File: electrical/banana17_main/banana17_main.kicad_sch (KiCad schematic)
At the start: 26 parts, among them J1 78171-0004, U1 RP2040, U2 NCP1117-3.3_SOT223, U3 ssd1306_128x32, U4 W25Q128JVS, Y1 ABMB-272-T3

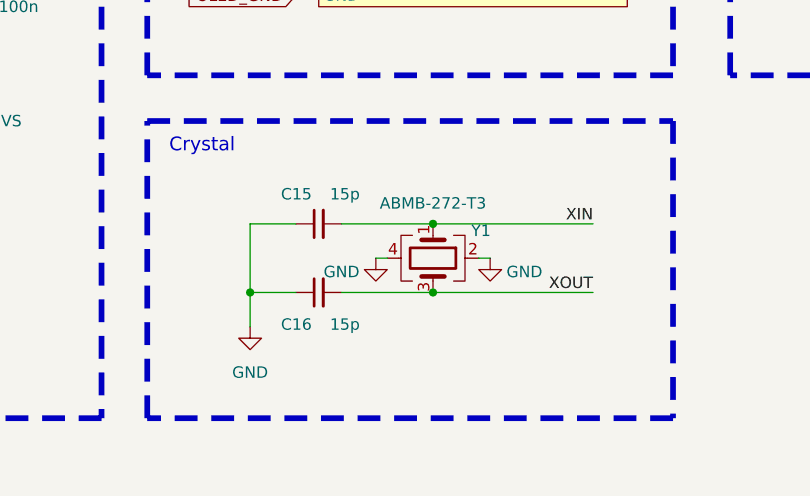
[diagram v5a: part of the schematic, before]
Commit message: MX footprint updated with hotswappable socket.
MX footprint updated with hotswappable socket. Some issues with KiCAD plugin for keyboard layout editor, switches not aligning.
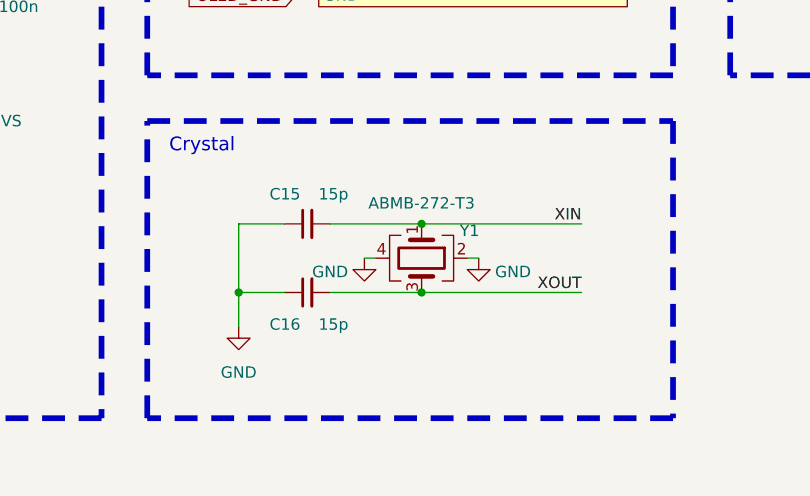
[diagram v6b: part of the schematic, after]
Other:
- moved on the sheet: C15, C16, Y1
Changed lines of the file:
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@@
 	)
 	(junction
-		(at 132.08 166.37)
+		(at 130.81 166.37)
 		(diameter 0)
 		(color 0 0 0 0)
@@
 	)
 	(junction
-		(at 132.08 173.99)
+		(at 130.81 173.99)
 		(diameter 0)
 		(color 0 0 0 0)
@@
 	)
 	(junction
-		(at 111.76 173.99)
+		(at 110.49 173.99)
 		(diameter 0)
 		(color 0 0 0 0)
@@
 	(wire
 		(pts
-			(xy 132.08 173.99) (xy 149.86 173.99)
+			(xy 130.81 173.99) (xy 148.59 173.99)
 		)
 		(stroke
@@
 	(wire
 		(pts
-			(xy 111.76 173.99) (xy 111.76 166.37)
+			(xy 110.49 173.99) (xy 110.49 166.37)
 		)
 		(stroke
@@
 	(wire
 		(pts
-			(xy 132.08 166.37) (xy 149.86 166.37)
+			(xy 130.81 166.37) (xy 148.59 166.37)
 		)
 		(stroke
@@
 	(wire
 		(pts
-			(xy 111.76 173.99) (xy 111.76 177.8)
+			(xy 110.49 173.99) (xy 110.49 177.8)
 		)
 		(stroke
@@
 	(wire
 		(pts
-			(xy 121.92 173.99) (xy 132.08 173.99)
+			(xy 120.65 173.99) (xy 130.81 173.99)
 		)
 		(stroke
@@
 	(wire
 		(pts
-			(xy 137.16 170.18) (xy 138.43 170.18)
+			(xy 135.89 170.18) (xy 137.16 170.18)
 		)
 		(stroke
@@
 	(wire
 		(pts
-			(xy 111.76 166.37) (xy 116.84 166.37)
+			(xy 110.49 166.37) (xy 115.57 166.37)
 		)
 		(stroke
@@
 	(wire
 		(pts
-			(xy 116.84 173.99) (xy 111.76 173.99)
+			(xy 115.57 173.99) (xy 110.49 173.99)
 		)
 		(stroke
@@
 	(wire
 		(pts
-			(xy 127 170.18) (xy 125.73 170.18)
+			(xy 125.73 170.18) (xy 124.46 170.18)
 		)
 		(stroke
@@
 	(wire
 		(pts
-			(xy 121.92 166.37) (xy 132.08 166.37)
+			(xy 120.65 166.37) (xy 130.81 166.37)
 		)
 		(stroke
@@
 	)
 	(label "XOUT"
-		(at 149.86 173.99 180)
+		(at 148.59 173.99 180)
 		(fields_autoplaced yes)
 		(effects
@@
 	)
 	(label "XIN"
-		(at 149.86 166.37 180)
+		(at 148.59 166.37 180)
 		(fields_autoplaced yes)
 		(effects
@@
 	(symbol
 		(lib_id "Device:Crystal_GND24")
-		(at 132.08 170.18 270)
+		(at 130.81 170.18 270)
 		(unit 1)
 		(exclude_from_sim no)
@@
 		(dnp no)
 		(property "Reference" "Y1"
-			(at 137.414 167.132 90)
+			(at 136.144 167.132 90)
 			(effects
 				(font
@@
 		)
 		(property "Value" "ABMB-272-T3"
-			(at 132.08 164.084 90)
+			(at 130.81 164.084 90)
 			(effects
 				(font
@@
 		)
 		(property "Footprint" "Crystal:Crystal_SMD_Abracon_ABM8G-4Pin_3.2x2.5mm"
-			(at 132.08 170.18 0)
+			(at 130.81 170.18 0)
 			(effects
 				(font
@@
 		)
 		(property "Datasheet" "~"
-			(at 132.08 170.18 0)
+			(at 130.81 170.18 0)
 			(effects
 				(font
@@
 		)
 		(property "Description" "Four pin crystal, GND on pins 2 and 4"
-			(at 132.08 170.18 0)
+			(at 130.81 170.18 0)
 			(effects
 				(font
@@
 	(symbol
 		(lib_id "power:GND")
-		(at 111.76 177.8 0)
+		(at 110.49 177.8 0)
 		(unit 1)
 		(exclude_from_sim no)
@@
 		(dnp no)
 		(property "Reference" "#PWR021"
-			(at 111.76 184.15 0)
+			(at 110.49 184.15 0)
 			(effects
 				(font
@@
 		)
 		(property "Value" "GND"
-			(at 111.76 182.88 0)
+			(at 110.49 182.88 0)
 			(effects
 				(font
@@
 		)
 		(property "Footprint" ""
-			(at 111.76 177.8 0)
+			(at 110.49 177.8 0)
 			(effects
 				(font
@@
 		)
 		(property "Datasheet" ""
-			(at 111.76 177.8 0)
+			(at 110.49 177.8 0)
 			(effects
 				(font
@@
 		)
 		(property "Description" "Power symbol creates a global label with name \"GND\" , ground"
-			(at 111.76 177.8 0)
+			(at 110.49 177.8 0)
 			(effects
 				(font
@@
 	(symbol
 		(lib_id "power:GND")
-		(at 138.43 170.18 0)
+		(at 137.16 170.18 0)
 		(unit 1)
 		(exclude_from_sim no)
@@
 		(dnp no)
 		(property "Reference" "#PWR018"
-			(at 138.43 176.53 0)
+			(at 137.16 176.53 0)
 			(effects
 				(font
@@
 		)
 		(property "Value" "GND"
-			(at 142.24 171.704 0)
+			(at 140.97 171.704 0)
 			(effects
 				(font
@@
 		)
 		(property "Footprint" ""
-			(at 138.43 170.18 0)
+			(at 137.16 170.18 0)
 			(effects
 				(font
@@
 		)
 		(property "Datasheet" ""
-			(at 138.43 170.18 0)
+			(at 137.16 170.18 0)
 			(effects
 				(font
@@
 		)
 		(property "Description" "Power symbol creates a global label with name \"GND\" , ground"
-			(at 138.43 170.18 0)
+			(at 137.16 170.18 0)
 			(effects
 				(font
@@
 	(symbol
 		(lib_id "power:GND")
-		(at 125.73 170.18 0)
+		(at 124.46 170.18 0)
 		(mirror y)
 		(unit 1)
@@
 		(dnp no)
 		(property "Reference" "#PWR017"
-			(at 125.73 176.53 0)
+			(at 124.46 176.53 0)
 			(effects
 				(font
@@
 		)
 		(property "Value" "GND"
-			(at 121.92 171.704 0)
+			(at 120.65 171.704 0)
 			(effects
 				(font
@@
 		)
 		(property "Footprint" ""
-			(at 125.73 170.18 0)
+			(at 124.46 170.18 0)
 			(effects
 				(font
@@
 		)
 		(property "Datasheet" ""
-			(at 125.73 170.18 0)
+			(at 124.46 170.18 0)
 			(effects
 				(font
@@
 		)
 		(property "Description" "Power symbol creates a global label with name \"GND\" , ground"
-			(at 125.73 170.18 0)
+			(at 124.46 170.18 0)
 			(effects
 				(font
@@
 	(symbol
 		(lib_id "Device:C_Small")
-		(at 119.38 166.37 90)
+		(at 118.11 166.37 90)
 		(unit 1)
 		(exclude_from_sim no)
@@
 		(dnp no)
 		(property "Reference" "C15"
-			(at 118.618 163.068 90)
+			(at 117.348 163.068 90)
 			(effects
 				(font
@@
 		)
 		(property "Value" "15p"
-			(at 123.952 163.068 90)
+			(at 122.682 163.068 90)
 			(effects
 				(font
@@
 		)
 		(property "Footprint" "Capacitor_SMD:C_0805_2012Metric_Pad1.18x1.45mm_HandSolder"
-			(at 119.38 166.37 0)
+			(at 118.11 166.37 0)
 			(effects
 				(font
@@
 		)
 		(property "Datasheet" "~"
-			(at 119.38 166.37 0)
+			(at 118.11 166.37 0)
 			(effects
 				(font
@@
 		)
 		(property "Description" "Unpolarized capacitor, small symbol"
-			(at 119.38 166.37 0)
+			(at 118.11 166.37 0)
 			(effects
 				(font
@@
 	(symbol
 		(lib_id "Device:C_Small")
-		(at 119.38 173.99 90)
+		(at 118.11 173.99 90)
 		(unit 1)
 		(exclude_from_sim no)
@@
 		(dnp no)
 		(property "Reference" "C16"
-			(at 118.618 177.546 90)
+			(at 117.348 177.546 90)
 			(effects
 				(font
@@
 		)
 		(property "Value" "15p"
-			(at 123.952 177.546 90)
+			(at 122.682 177.546 90)
 			(effects
 				(font
@@
 		)
 		(property "Footprint" "Capacitor_SMD:C_0805_2012Metric_Pad1.18x1.45mm_HandSolder"
-			(at 119.38 173.99 0)
+			(at 118.11 173.99 0)
 			(effects
 				(font
@@
 		)
 		(property "Datasheet" "~"
-			(at 119.38 173.99 0)
+			(at 118.11 173.99 0)
 			(effects
 				(font
@@
 		)
 		(property "Description" "Unpolarized capacitor, small symbol"
-			(at 119.38 173.99 0)
+			(at 118.11 173.99 0)
 			(effects
 				(font

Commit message: Switches positioned in matrix. Working on positioning the RP2040.
Switches positioned in matrix. Working on positioning the RP2040.
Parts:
- C1, C10, C11, C2, C3, C4, C5, C6, C7, C8, C9: footprint Capacitor_SMD:C_0805_2012Metric_Pad1.18x1.45mm_HandSolder -> Capacitor_SMD:C_0402_1005Metric_Pad0.74x0.62mm_HandSolder
- R1, R2: footprint Resistor_SMD:R_0805_2012Metric_Pad1.20x1.40mm_HandSolder -> Resistor_SMD:R_0402_1005Metric_Pad0.72x0.64mm_HandSolder
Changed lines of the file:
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@@
 	)
 	(junction
-		(at 135.89 46.99)
-		(diameter 0)
-		(color 0 0 0 0)
-	)
-	(junction
 		(at 105.41 39.37)
 		(diameter 0)
@@
 	)
 	(junction
-		(at 135.89 39.37)
+		(at 135.89 46.99)
 		(diameter 0)
 		(color 0 0 0 0)
@@
 		(color 0 0 0 0)
 	)
+	(junction
+		(at 135.89 39.37)
+		(diameter 0)
+		(color 0 0 0 0)
+	)
 	(wire
 		(pts
@@
 	(wire
 		(pts
+			(xy 135.89 46.99) (xy 146.05 46.99)
+		)
+		(stroke
+			(width 0)
+			(type default)
+		)
+	)
+	(wire
+		(pts
 			(xy 130.81 173.99) (xy 148.59 173.99)
 		)
@@
 	(wire
 		(pts
-			(xy 146.05 40.64) (xy 146.05 39.37)
-		)
-		(stroke
-			(width 0)
-			(type default)
-		)
-	)
-	(wire
-		(pts
 			(xy 248.92 60.96) (xy 265.43 60.96)
 		)
@@
 	(wire
 		(pts
-			(xy 146.05 39.37) (xy 135.89 39.37)
-		)
-		(stroke
-			(width 0)
-			(type default)
-		)
-	)
-	(wire
-		(pts
 			(xy 55.88 39.37) (xy 55.88 40.64)
 		)
@@
 	(wire
 		(pts
+			(xy 135.89 39.37) (xy 146.05 39.37)
+		)
+		(stroke
+			(width 0)
+			(type default)
+		)
+	)
+	(wire
+		(pts
 			(xy 45.72 39.37) (xy 45.72 40.64)
 		)
@@
 	(wire
 		(pts
+			(xy 146.05 39.37) (xy 146.05 40.64)
+		)
+		(stroke
+			(width 0)
+			(type default)
+		)
+	)
+	(wire
+		(pts
 			(xy 81.28 135.89) (xy 66.04 135.89)
 		)
@@
 	(wire
 		(pts
+			(xy 146.05 45.72) (xy 146.05 46.99)
+		)
+		(stroke
+			(width 0)
+			(type default)
+		)
+	)
+	(wire
+		(pts
 			(xy 110.49 36.83) (xy 110.49 39.37)
 		)
@@
 	(wire
 		(pts
-			(xy 135.89 46.99) (xy 146.05 46.99)
-		)
-		(stroke
-			(width 0)
-			(type default)
-		)
-	)
-	(wire
-		(pts
 			(xy 76.2 39.37) (xy 76.2 40.64)
 		)
@@
 	(wire
 		(pts
-			(xy 146.05 46.99) (xy 146.05 45.72)
-		)
-		(stroke
-			(width 0)
-			(type default)
-		)
-	)
-	(wire
-		(pts
 			(xy 248.92 121.92) (xy 265.43 121.92)
 		)
@@
 			)
 		)
-		(property "Footprint" "Capacitor_SMD:C_0805_2012Metric_Pad1.18x1.45mm_HandSolder"
+		(property "Footprint" "Capacitor_SMD:C_0402_1005Metric_Pad0.74x0.62mm_HandSolder"
 			(at 96.52 43.18 0)
 			(effects
@@
 			)
 		)
-		(property "Footprint" "Capacitor_SMD:C_0805_2012Metric_Pad1.18x1.45mm_HandSolder"
+		(property "Footprint" "Capacitor_SMD:C_0402_1005Metric_Pad0.74x0.62mm_HandSolder"
 			(at 105.41 43.18 0)
 			(effects
@@
 			)
 		)
-		(property "Footprint" "Capacitor_SMD:C_0805_2012Metric_Pad1.18x1.45mm_HandSolder"
+		(property "Footprint" "Capacitor_SMD:C_0402_1005Metric_Pad0.74x0.62mm_HandSolder"
 			(at 55.88 43.18 0)
 			(effects
@@
 			)
 		)
-		(property "Footprint" "Capacitor_SMD:C_0805_2012Metric_Pad1.18x1.45mm_HandSolder"
+		(property "Footprint" "Capacitor_SMD:C_0402_1005Metric_Pad0.74x0.62mm_HandSolder"
 			(at 115.57 43.18 0)
 			(effects
@@
 			)
 		)
-		(property "Footprint" "Resistor_SMD:R_0805_2012Metric_Pad1.20x1.40mm_HandSolder"
+		(property "Footprint" "Resistor_SMD:R_0402_1005Metric_Pad0.72x0.64mm_HandSolder"
 			(at 186.69 55.88 0)
 			(effects
@@
 			)
 		)
-		(property "Footprint" "Resistor_SMD:R_0805_2012Metric_Pad1.20x1.40mm_HandSolder"
+		(property "Footprint" "Resistor_SMD:R_0402_1005Metric_Pad0.72x0.64mm_HandSolder"
 			(at 186.69 58.42 0)
 			(effects
@@
 	)
 	(symbol
+		(lib_id "Device:C_Small")
+		(at 146.05 43.18 0)
+		(unit 1)
+		(exclude_from_sim no)
+		(in_bom yes)
+		(on_board yes)
+		(dnp no)
+		(property "Reference" "C11"
+			(at 148.59 41.9162 0)
+			(effects
+				(font
+					(size 1.27 1.27)
+				)
+				(justify left)
+			)
+		)
+		(property "Value" "100n"
+			(at 148.59 44.45 0)
+			(effects
+				(font
+					(size 1.27 1.27)
+				)
+				(justify left)
+			)
+		)
+		(property "Footprint" "Capacitor_SMD:C_0402_1005Metric_Pad0.74x0.62mm_HandSolder"
+			(at 146.05 43.18 0)
+			(effects
+				(font
+					(size 1.27 1.27)
+				)
+				(hide yes)
+			)
+		)
+		(property "Datasheet" "~"
+			(at 146.05 43.18 0)
+			(effects
+				(font
+					(size 1.27 1.27)
+				)
+				(hide yes)
+			)
+		)
+		(property "Description" "Unpolarized capacitor, small symbol"
+			(at 146.05 43.18 0)
+			(effects
+				(font
+					(size 1.27 1.27)
+				)
+				(hide yes)
+			)
+		)
+		(pin "1"
+		)
+		(pin "2"
+		)
+		(instances
+			(project "banana17_main"
+				(path "/fd2b462c-d7c2-4bbf-9a41-8b3fef737a65"
+					(reference "C11")
+					(unit 1)
+				)
+			)
+		)
+	)
+	(symbol
 		(lib_id "power:VBUS")
 		(at 139.7 87.63 0)
@@
 			)
 		)
-		(property "Footprint" "Capacitor_SMD:C_0805_2012Metric_Pad1.18x1.45mm_HandSolder"
+		(property "Footprint" "Capacitor_SMD:C_0402_1005Metric_Pad0.74x0.62mm_HandSolder"
 			(at 35.56 43.18 0)
 			(effects
@@
 			)
 		)
-		(property "Footprint" "Capacitor_SMD:C_0805_2012Metric_Pad1.18x1.45mm_HandSolder"
+		(property "Footprint" "Capacitor_SMD:C_0402_1005Metric_Pad0.74x0.62mm_HandSolder"
 			(at 86.36 43.18 0)
 			(effects
@@
 	)
 	(symbol
-		(lib_id "Device:C_Small")
-		(at 146.05 43.18 0)
-		(unit 1)
-		(exclude_from_sim no)
-		(in_bom yes)
-		(on_board yes)
-		(dnp no)
-		(property "Reference" "C11"
-			(at 148.59 41.9162 0)
-			(effects
-				(font
-					(size 1.27 1.27)
-				)
-				(justify left)
-			)
-		)
-		(property "Value" "100n"
-			(at 148.59 44.45 0)
-			(effects
-				(font
-					(size 1.27 1.27)
-				)
-				(justify left)
-			)
-		)
-		(property "Footprint" "Capacitor_SMD:C_0805_2012Metric_Pad1.18x1.45mm_HandSolder"
-			(at 146.05 43.18 0)
-			(effects
-				(font
-					(size 1.27 1.27)
-				)
-				(hide yes)
-			)
-		)
-		(property "Datasheet" "~"
-			(at 146.05 43.18 0)
-			(effects
-				(font
-					(size 1.27 1.27)
-				)
-				(hide yes)
-			)
-		)
-		(property "Description" "Unpolarized capacitor, small symbol"
-			(at 146.05 43.18 0)
-			(effects
-				(font
-					(size 1.27 1.27)
-				)
-				(hide yes)
-			)
-		)
-		(pin "1"
-		)
-		(pin "2"
-		)
-		(instances
-			(project "banana17_main"
-				(path "/fd2b462c-d7c2-4bbf-9a41-8b3fef737a65"
-					(reference "C11")
-					(unit 1)
-				)
-			)
-		)
-	)
-	(symbol
 		(lib_id "power:VBUS")
 		(at 31.75 91.44 0)
@@
 			)
 		)
-		(property "Footprint" "Capacitor_SMD:C_0805_2012Metric_Pad1.18x1.45mm_HandSolder"
+		(property "Footprint" "Capacitor_SMD:C_0402_1005Metric_Pad0.74x0.62mm_HandSolder"
 			(at 135.89 43.18 0)
 			(effects
@@
 			)
 		)
-		(property "Footprint" "Capacitor_SMD:C_0805_2012Metric_Pad1.18x1.45mm_HandSolder"
+		(property "Footprint" "Capacitor_SMD:C_0402_1005Metric_Pad0.74x0.62mm_HandSolder"
 			(at 45.72 43.18 0)
 			(effects
@@
 			)
 		)
-		(property "Footprint" "Capacitor_SMD:C_0805_2012Metric_Pad1.18x1.45mm_HandSolder"
+		(property "Footprint" "Capacitor_SMD:C_0402_1005Metric_Pad0.74x0.62mm_HandSolder"
 			(at 76.2 43.18 0)
 			(effects
@@
 			)
 		)
-		(property "Footprint" "Capacitor_SMD:C_0805_2012Metric_Pad1.18x1.45mm_HandSolder"
+		(property "Footprint" "Capacitor_SMD:C_0402_1005Metric_Pad0.74x0.62mm_HandSolder"
 			(at 125.73 43.18 0)
 			(effects

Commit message: General layout complete.
General layout complete.
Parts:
- C12, C13, C14, C15, C16: footprint Capacitor_SMD:C_0805_2012Metric_Pad1.18x1.45mm_HandSolder -> Capacitor_SMD:C_0402_1005Metric_Pad0.74x0.62mm_HandSolder
- R3: footprint Resistor_SMD:R_0805_2012Metric_Pad1.20x1.40mm_HandSolder -> Resistor_SMD:R_0402_1005Metric_Pad0.72x0.64mm_HandSolder
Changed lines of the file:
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@@
 			)
 		)
-		(property "Footprint" "Capacitor_SMD:C_0805_2012Metric_Pad1.18x1.45mm_HandSolder"
+		(property "Footprint" "Capacitor_SMD:C_0402_1005Metric_Pad0.74x0.62mm_HandSolder"
 			(at 40.3352 101.6 0)
 			(effects
@@
 			)
 		)
-		(property "Footprint" "Capacitor_SMD:C_0805_2012Metric_Pad1.18x1.45mm_HandSolder"
+		(property "Footprint" "Capacitor_SMD:C_0402_1005Metric_Pad0.74x0.62mm_HandSolder"
 			(at 81.28 140.97 0)
 			(effects
@@
 			)
 		)
-		(property "Footprint" "Capacitor_SMD:C_0805_2012Metric_Pad1.18x1.45mm_HandSolder"
+		(property "Footprint" "Capacitor_SMD:C_0402_1005Metric_Pad0.74x0.62mm_HandSolder"
 			(at 118.11 166.37 0)
 			(effects
@@
 			)
 		)
-		(property "Footprint" "Capacitor_SMD:C_0805_2012Metric_Pad1.18x1.45mm_HandSolder"
+		(property "Footprint" "Capacitor_SMD:C_0402_1005Metric_Pad0.74x0.62mm_HandSolder"
 			(at 118.11 173.99 0)
 			(effects
@@
 			)
 		)
-		(property "Footprint" "Resistor_SMD:R_0805_2012Metric_Pad1.20x1.40mm_HandSolder"
+		(property "Footprint" "Resistor_SMD:R_0402_1005Metric_Pad0.72x0.64mm_HandSolder"
 			(at 34.798 151.13 90)
 			(effects
@@
 			)
 		)
-		(property "Footprint" "Capacitor_SMD:C_0805_2012Metric_Pad1.18x1.45mm_HandSolder"
+		(property "Footprint" "Capacitor_SMD:C_0402_1005Metric_Pad0.74x0.62mm_HandSolder"
 			(at 80.9752 101.6 0)
 			(effects
